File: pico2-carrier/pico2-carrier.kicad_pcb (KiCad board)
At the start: 4 copper layers, 75 x 75 mm, 65 parts, among them IC1 TFDU4101-TT3, IC2 M95512-DWDW4TP_K, IC3 W25Q128JVSIM_TR, IC4 BQ25628ERYKR, J2 DO0180FMST08, J3 Ext_Pwr_Rail, Q1 DMG2305UX-7, SW1 RUN, SW5 BUT_L, SW6 BUT_M, SW7 BUT_R, U1 Pico 2

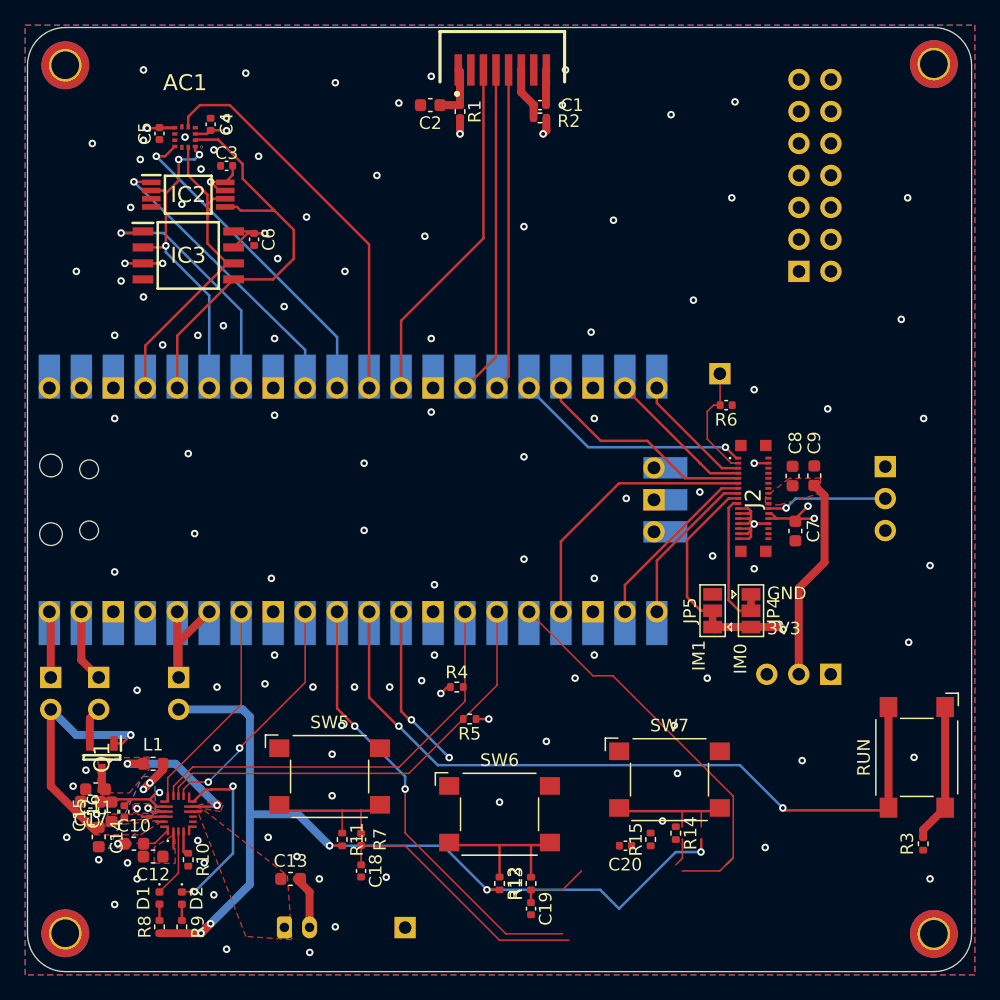
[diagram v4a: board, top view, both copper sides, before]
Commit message: carrier: update PMIC layout and button filters
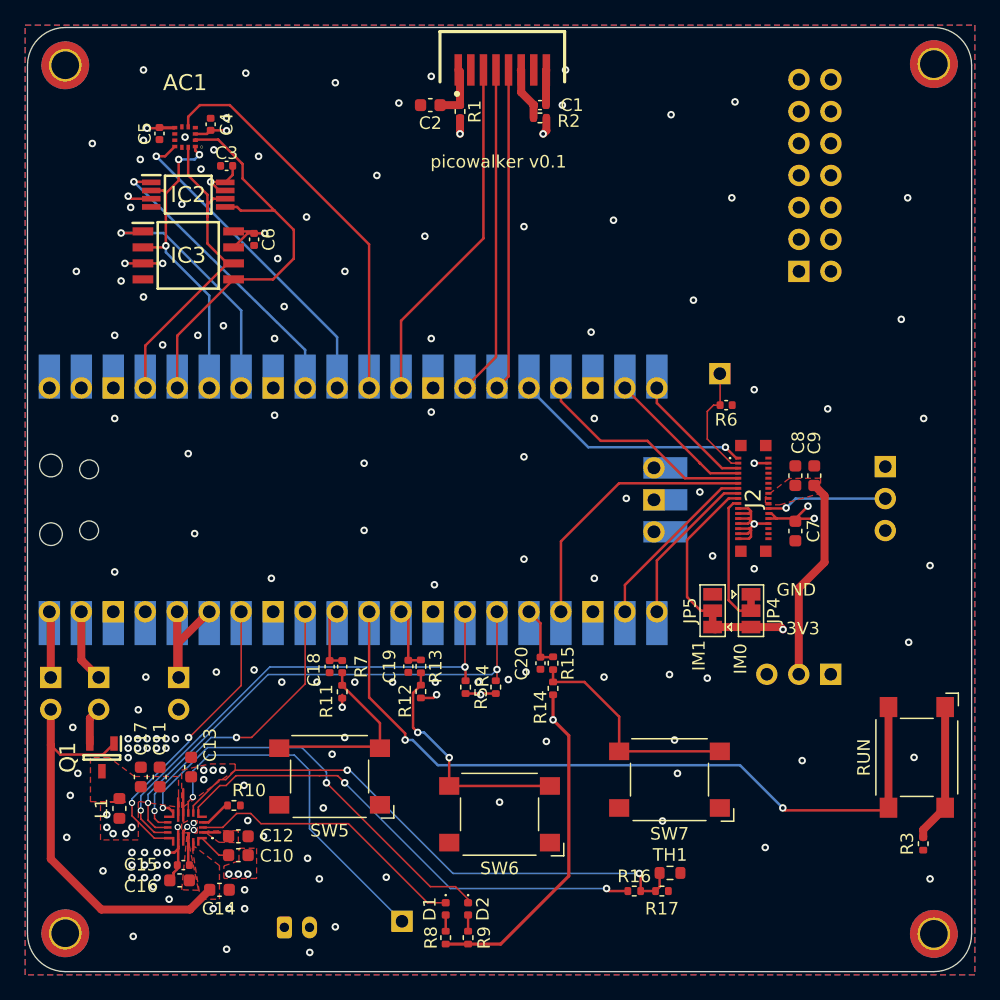
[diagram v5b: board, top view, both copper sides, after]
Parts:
- added R16: R, Resistor_SMD:R_0402_1005Metric, F.Cu at (163.7, 132.7)
- added R17: R, Resistor_SMD:R_0402_1005Metric, F.Cu at (165.9, 132.7)
- added TH1: 10k, Resistor_SMD:R_0603_1608Metric, F.Cu at (166.5, 131.3)
- moved D1 22.8 mm to (148.7, 134.1)
- moved R8 22.8 mm to (148.7, 136.4)
- moved D2 22.8 mm to (150.5, 134.1)
- moved R9 22.8 mm to (150.5, 136.4)
- moved C19 21.6 mm to (145.8, 114.8)
- moved R13 19.3 mm to (146.8, 114.8), turned to -90 degrees
- moved R12 16.5 mm to (146.8, 116.8)
- moved C18 16.4 mm to (139.5, 114.9)
- moved R15 16.0 mm to (157.2, 114.6), turned to -90 degrees
- moved C20 16.0 mm to (156.2, 114.6), turned to -90 degrees
- moved R14 15.1 mm to (157.2, 116.6)
- moved R7 13.8 mm to (140.5, 114.9), turned to -90 degrees
- moved C13 11.9 mm to (128.5, 122.8), turned to 90 degrees
- moved R11 11.7 mm to (140.5, 116.9)
- moved C14 10.5 mm to (130.8, 132.6), turned to 0 degrees
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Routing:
- net /BUT_L: track 57.1 -> 5.12 mm, vias 2 -> 0
- net /battery-bq25628e/TS: track 0.00 -> 44.8 mm, vias 0 -> 2
- net +3.3V: track 107.6 -> 66.2 mm, vias 18 -> 16
- net /battery-bq25628e/TS_BIAS: track 0.00 -> 39.4 mm, vias 0 -> 2
- net /BUT_R: track 34.7 -> 5.00 mm
- net /battery-bq25628e/~{QON}: track 0.00 -> 28.8 mm, vias 0 -> 1
- net /battery-bq25628e/STAT: track 14.3 -> 33.7 mm
- net /battery-bq25628e/~{PG}: track 5.44 -> 22.7 mm
- net /BUT_M: track 19.3 -> 5.11 mm, vias 2 -> 0
- net VBUS: track 20.6 -> 33.2 mm, vias 1 -> 0
- net /battery-bq25628e/SYS: track 13.3 -> 1.38 mm, vias 2 -> 0
- net /buttons-debounce/BUT_R_1: track 10.5 -> 18.1 mm
- net /~{BAT_CE}: track 17.2 -> 23.5 mm, vias 0 -> 2
- net /I2C_SDA: track 35.2 -> 41.2 mm, vias 0 -> 2
- net /I2C_SCL: track 33.9 -> 39.8 mm, vias 0 -> 2
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- added copper zone on In2.Cu, net /battery-bq25628e/BAT+
- added copper zone on In2.Cu, net /battery-bq25628e/SW
- removed copper zone on B.Cu, net /battery-bq25628e/SW
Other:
- board text added: "+"
- board text added: "-"
- board text added: "picowalker v0.1"
- board text removed: "BAT+"
- board text removed: "BAT-"

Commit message: carrier: update ir footprint
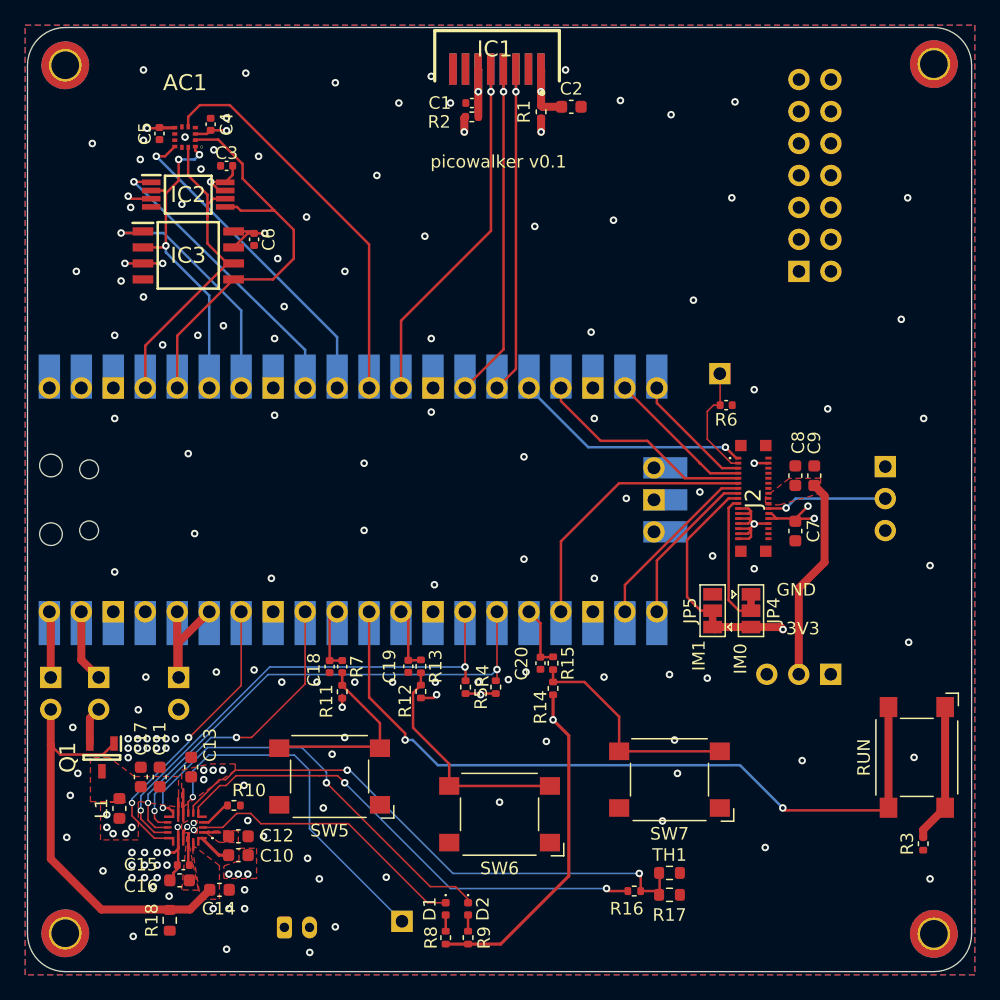
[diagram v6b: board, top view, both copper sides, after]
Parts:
- added R18: 100k, Resistor_SMD:R_0603_1608Metric, F.Cu at (126.8, 135.0)
- IC1: footprint SamacsysParts:TFDU4101-TR3 -> SamacsysParts:TFDU4101-TR3-TopBottom
- R16: value R -> 5.3k
- R17: value R -> 30k; footprint Resistor_SMD:R_0402_1005Metric -> Resistor_SMD:R_0603_1608Metric
- moved C2 11.2 mm to (158.7, 70.4), turned to 0 degrees
- moved R1 6.44 mm to (156.3, 70.8)
- moved C1 5.41 mm to (150.8, 70.1), turned to 0 degrees
- moved R2 5.41 mm to (150.8, 71.2), turned to 0 degrees
- moved R17 0.67 mm to (166.5, 133.0)
- moved IC1 0.64 mm to (147.7, 68.7)
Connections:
- U1 pad 12: /IR_PIO_TX -> /IR_SD
- U1 pad 15: /IR_SD -> /IR_PIO_TX
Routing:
- net /IR_SD: track 25.6 -> 29.4 mm, vias 0 -> 1
- net GND: track 20.9 -> 18.1 mm, vias 138 -> 139
- net /VCC2: track 4.15 -> 6.22 mm, vias 0 -> 1
- net /IR_PIO_RX: track 26.3 -> 27.7 mm, vias 0 -> 1
- net /VCC1: track 4.29 -> 5.46 mm, vias 0 -> 1
- net /IR_PIO_TX: track 28.0 -> 27.6 mm, vias 0 -> 1
- net /buttons-debounce/BUT_M_1: track 18.7 -> 18.4 mm, vias 2 -> 0

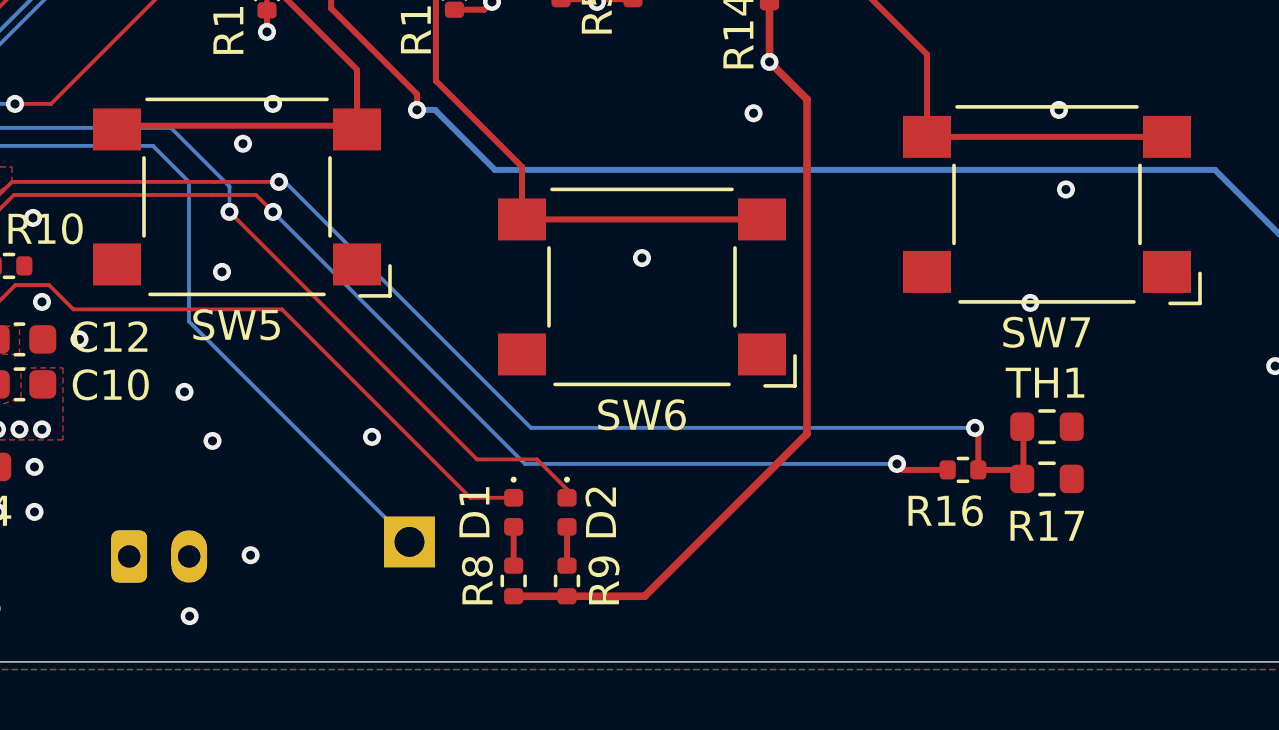
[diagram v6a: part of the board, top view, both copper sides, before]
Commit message: carrier: move thermistor to back of board and clear space for battery
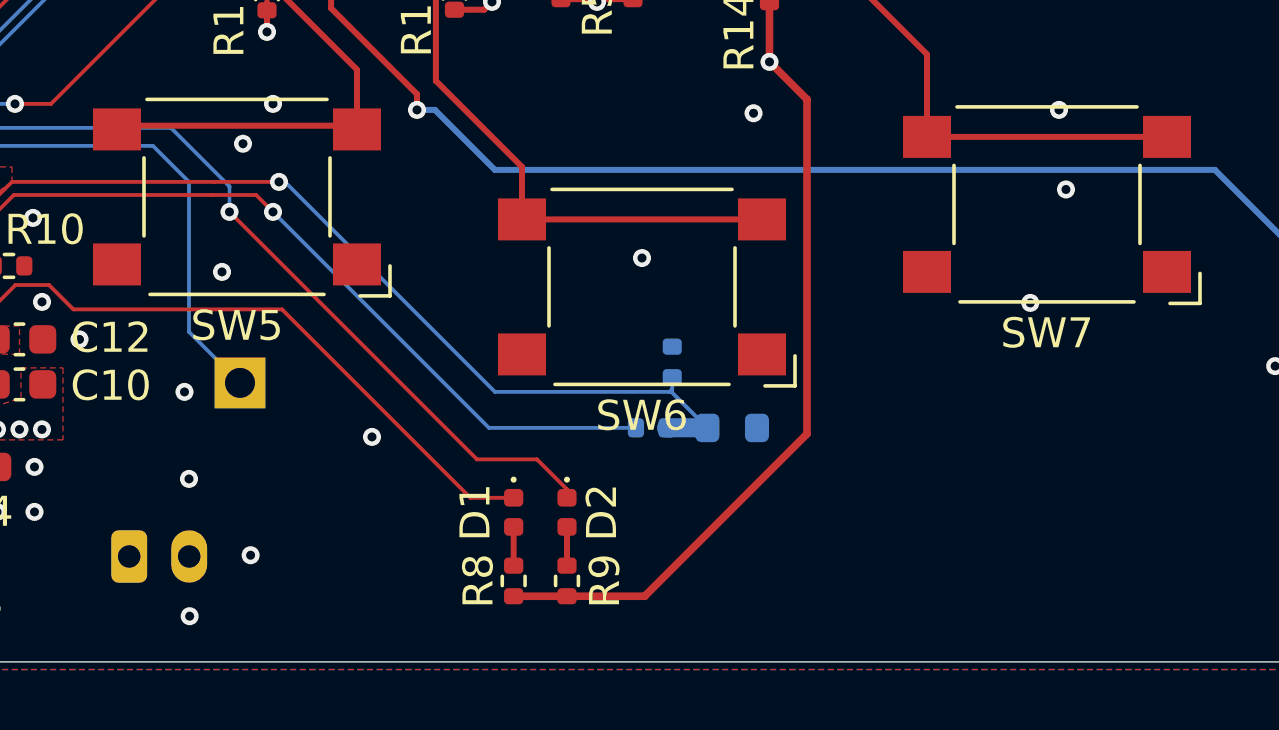
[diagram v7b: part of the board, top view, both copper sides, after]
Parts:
- R16, R17: moved to B.Cu
- TH1: footprint Resistor_SMD:R_0603_1608Metric -> Resistor_SMD:R_0402_1005Metric; moved to B.Cu
- moved TH1 12.7 mm to (154.0, 129.1), turned to 90 degrees
- moved R17 10.6 mm to (156.0, 131.3)
- moved R16 10.5 mm to (153.3, 131.3)
- moved TP1 7.75 mm to (139.6, 129.8)
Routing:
- net /battery-bq25628e/TS: track 45.0 -> 33.5 mm, vias 2 -> 1
- net /battery-bq25628e/TS_BIAS: track 39.4 -> 28.4 mm, vias 2 -> 1
- net /battery-bq25628e/~{QON}: track 28.8 -> 21.2 mm
